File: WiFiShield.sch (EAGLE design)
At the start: 39 parts, among them IC1 74HC4050D, IC2 74AHC1G125, IC3 MCP9701A, IC4 SPX3819M5-L-3-3, IC5 CC3000MOD, J10 Test, J2 Mode, J3 Temp, J8 ARDUINO-SHIELD_R3, J9 U.FL-R-SMT-1(10)

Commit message: Fixups for MC74VHCT
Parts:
- IC1: value 74HC4050D -> MC74VHCT50A
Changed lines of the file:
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@@
 <part name="ANT1" library="adafruit" deviceset="ANTENNA" device=""/>
 <part name="U$2" library="freetronics-luke" deviceset="GND" device=""/>
-<part name="IC1" library="freetronics-angus" deviceset="MC74VHCT50A" device="" value="74HC4050D">
+<part name="IC1" library="freetronics-angus" deviceset="MC74VHCT50A" device="" value="MC74VHCT50A">
 <attribute name="PACKAGE" value="16-SOIC"/>
 </part>

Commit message: Remove temp sensor
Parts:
- removed IC3: MCP9701A, freetronics-master-v1:MCP9700SOT-23
- removed J3: Temp, freetronics-luke:SJ
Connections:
- removed net +5V-2: IC3.VDD, J8.+5V@0
- removed net N$11: IC3.OUT, J3.1
- new net N$3: IC1E.O
- net A0: no longer J3.2
- net CC3000_EN_3V3: no longer IC1E.O
- net GND: no longer IC3.GND
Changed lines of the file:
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@@
 <part name="J4" library="freetronics-master-v1.1" deviceset="M04" device="PTH"/>
 <part name="U$8" library="freetronics-luke" deviceset="+3.3V" device="" value="+3V3"/>
-<part name="IC3" library="freetronics-master-v1" deviceset="MCP9700" device="SOT-23" value="MCP9701A">
-<attribute name="PACKAGE" value="3-SOT23"/>
-</part>
-<part name="J3" library="freetronics-luke" deviceset="SJ" device="" value="Temp"/>
 <part name="S1" library="freetronics" deviceset="TAC_SWITCH" device="SMD" value="Reset"/>
-<part name="U$6" library="freetronics-luke" deviceset="GND" device=""/>
-<part name="U$9" library="freetronics-luke" deviceset="+5V" device=""/>
-<part name="U$11" library="freetronics-luke" deviceset="+5V" device=""/>
 <part name="U$12" library="freetronics-luke" deviceset="+3.3V" device="" value="+3V3"/>
 <part name="R5" library="freetronics-master-v1" deviceset="RESISTOR" device="0603" value="10k">
@@
 <attribute name="VALUE" x="40.64" y="175.26" size="1.27" layer="96" rot="MR0"/>
 </instance>
-<instance part="IC3" gate="G$1" x="88.9" y="20.32" smashed="yes">
-<attribute name="PACKAGE" x="76.2" y="30.48" size="1.27" layer="96"/>
-<attribute name="VALUE" x="76.2" y="33.02" size="1.27" layer="96"/>
-<attribute name="NAME" x="76.2" y="35.56" size="1.27" layer="95"/>
-</instance>
-<instance part="J3" gate="G$1" x="101.6" y="20.32" smashed="yes">
-<attribute name="NAME" x="101.6" y="15.24" size="1.27" layer="95"/>
-<attribute name="VALUE" x="101.6" y="12.7" size="1.27" layer="96"/>
-</instance>
 <instance part="S1" gate="S" x="218.44" y="101.6" smashed="yes">
 <attribute name="NAME" x="228.6" y="101.6" size="1.27" layer="95"/>
 <attribute name="VALUE" x="228.6" y="99.06" size="1.27" layer="96"/>
 </instance>
-<instance part="U$6" gate="G$1" x="99.06" y="10.16"/>
-<instance part="U$9" gate="G$1" x="99.06" y="30.48" rot="MR0"/>
-<instance part="U$11" gate="G$1" x="228.6" y="165.1"/>
 <instance part="U$12" gate="G$1" x="129.54" y="35.56" smashed="yes" rot="MR0">
 <attribute name="VALUE" x="127" y="35.56" size="1.27" layer="96" rot="MR0"/>
@@
 </segment>
 <segment>
-<pinref part="IC3" gate="G$1" pin="GND"/>
-<wire x1="96.52" y1="15.24" x2="99.06" y2="15.24" width="0.1524" layer="91"/>
-<pinref part="U$6" gate="G$1" pin="GND"/>
-<wire x1="99.06" y1="15.24" x2="99.06" y2="12.7" width="0.1524" layer="91"/>
-</segment>
-<segment>
 <pinref part="IC2" gate="P" pin="GND"/>
 <wire x1="25.4" y1="165.1" x2="22.86" y2="165.1" width="0.1524" layer="91"/>
@@
 <wire x1="223.52" y1="132.08" x2="205.74" y2="132.08" width="0.1524" layer="91"/>
 <label x="210.82" y="132.334" size="1.27" layer="95"/>
-</segment>
-<segment>
-<pinref part="J3" gate="G$1" pin="2"/>
-<wire x1="104.14" y1="20.32" x2="111.76" y2="20.32" width="0.1524" layer="91"/>
-<label x="106.68" y="20.574" size="1.27" layer="95"/>
 </segment>
 </net>
@@
 <net name="CC3000_EN_3V3" class="0">
 <segment>
-<pinref part="IC1" gate="E" pin="O"/>
-<wire x1="60.96" y1="15.24" x2="71.12" y2="15.24" width="0.1524" layer="91"/>
-<wire x1="71.12" y1="15.24" x2="71.12" y2="40.64" width="0.1524" layer="91"/>
-<wire x1="71.12" y1="40.64" x2="137.16" y2="40.64" width="0.1524" layer="91"/>
 <wire x1="137.16" y1="40.64" x2="172.72" y2="40.64" width="0.1524" layer="91"/>
 <wire x1="172.72" y1="40.64" x2="172.72" y2="63.5" width="0.1524" layer="91"/>
@@
 <wire x1="129.54" y1="17.78" x2="137.16" y2="17.78" width="0.1524" layer="91"/>
 <wire x1="137.16" y1="17.78" x2="137.16" y2="40.64" width="0.1524" layer="91"/>
-<junction x="137.16" y="40.64"/>
 </segment>
 </net>
@@
 </segment>
 </net>
-<net name="N$11" class="0">
-<segment>
-<pinref part="IC3" gate="G$1" pin="OUT"/>
-<wire x1="96.52" y1="20.32" x2="99.06" y2="20.32" width="0.1524" layer="91"/>
-<pinref part="J3" gate="G$1" pin="1"/>
-</segment>
-</net>
-<net name="+5V-2" class="0">
-<segment>
-<pinref part="J8" gate="G$1" pin="+5V@0"/>
-<pinref part="U$11" gate="G$1" pin="+5V"/>
-<wire x1="205.74" y1="160.02" x2="228.6" y2="160.02" width="0.1524" layer="91"/>
-<wire x1="228.6" y1="160.02" x2="228.6" y2="162.56" width="0.1524" layer="91"/>
-</segment>
-<segment>
-<pinref part="IC3" gate="G$1" pin="VDD"/>
-<wire x1="96.52" y1="25.4" x2="99.06" y2="25.4" width="0.1524" layer="91"/>
-<pinref part="U$9" gate="G$1" pin="+5V"/>
-<wire x1="99.06" y1="25.4" x2="99.06" y2="27.94" width="0.1524" layer="91"/>
-</segment>
-</net>
 <net name="!CC3000_CS_5V" class="0">
 <segment>
@@
 </segment>
 </net>
+<net name="N$3" class="0">
+<segment>
+<wire x1="71.12" y1="15.24" x2="71.12" y2="40.64" width="0.1524" layer="91"/>
+<pinref part="IC1" gate="E" pin="O"/>
+<wire x1="60.96" y1="15.24" x2="71.12" y2="15.24" width="0.1524" layer="91"/>
+</segment>
+</net>

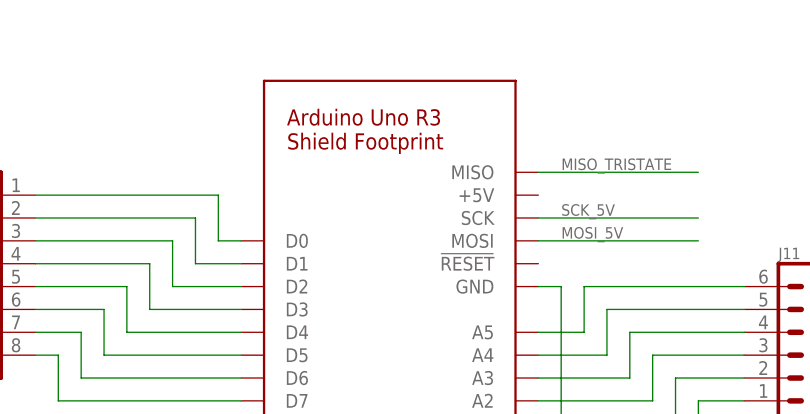
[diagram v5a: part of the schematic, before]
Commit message: Add silkscreen border
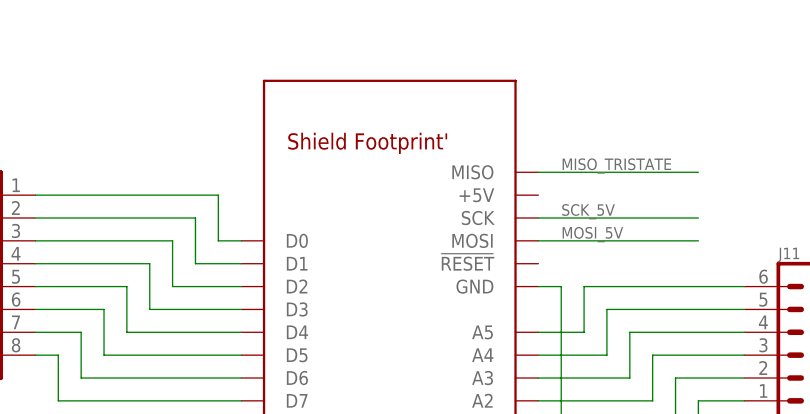
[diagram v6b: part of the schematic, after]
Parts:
- J8: device freetronics-luke:ARDUINO-SHIELD_R3 -> freetronics-angus:ARDUINO-SHIELD_R3
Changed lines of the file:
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@@
 </part>
 <part name="U$5" library="freetronics-luke" deviceset="GND" device=""/>
-<part name="J8" library="freetronics-luke" deviceset="ARDUINO-SHIELD_R3" device=""/>
+<part name="J8" library="freetronics-angus" deviceset="ARDUINO-SHIELD_R3" device=""/>
 <part name="U$21" library="freetronics-luke" deviceset="GND" device=""/>
 <part name="U$23" library="freetronics-luke" deviceset="GND" device=""/>

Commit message: Switch to chip antenna, final pre-prototype design review
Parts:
- removed R6, R7: 0R, freetronics-master-v1:RESISTOR0603
- ANT1: value ANTENNA -> 2500AT44M0400; device adafruit:ANTENNA -> freetronics-angus:2500AT44M0400
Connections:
- removed net N$15: IC5.SCL_CC3000, R6.2
- removed net N$5: IC5.SCL_EEPROM, R6.1
- net GND: no longer ANT1.GND
- net N$1: now also IC5.SDA_CC3000; no longer R7.2
- net N$104: now also ANT1.P$1; no longer ANT1.FEED
- net N$2: now also IC5.SCL_CC3000, IC5.SCL_EEPROM; no longer IC5.SDA_CC3000, R7.1
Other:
- note added: "50Ω 2.4 GHz Feed"
- note removed: "Meandered inverted-F antenna; 50Ω 2.4 GHz"
- moved on the sheet: J9
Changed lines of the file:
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@@
 <part name="IC5" library="freetronics-luke" deviceset="CC3000" device="" value="CC3000MOD"/>
 <part name="U$13" library="freetronics-luke" deviceset="GND" device=""/>
-<part name="R7" library="freetronics-master-v1" deviceset="RESISTOR" device="0603" value="0R">
-<attribute name="PACKAGE" value="0603"/>
-</part>
 <part name="C6" library="freetronics-master-v1" deviceset="CAP" device="0603" value="1uF">
 <attribute name="PACKAGE" value="0603"/>
 </part>
 <part name="+3V1" library="supply1" deviceset="+3V3" device="" value="+3V3"/>
-<part name="R6" library="freetronics-master-v1" deviceset="RESISTOR" device="0603" value="0R">
-<attribute name="PACKAGE" value="0603"/>
-</part>
 <part name="U$14" library="freetronics-luke" deviceset="GND" device=""/>
 <part name="L2" library="freetronics-master-v1" deviceset="INDUCTOR" device="0402" value="NP">
@@
 <attribute name="NOTE" value="NP"/>
 </part>
-<part name="ANT1" library="adafruit" deviceset="ANTENNA" device=""/>
 <part name="U$2" library="freetronics-luke" deviceset="GND" device=""/>
 <part name="IC1" library="freetronics-angus" deviceset="MC74VHCT50A" device="" value="MC74VHCT50A">
@@
 <part name="U$10" library="freetronics-luke" deviceset="GND" device=""/>
 <part name="U$27" library="freetronics-master-v1.1" deviceset="USD-SOCKET" device="NEW"/>
+<part name="ANT1" library="freetronics-angus" deviceset="2500AT44M0400" device=""/>
 </parts>
 <sheets>
@@
 <text x="68.58" y="88.9" size="1.27" layer="98">1-2: Test Mode
 2-3: Normal Mode</text>
-<text x="205.74" y="50.8" size="1.27" layer="98">Meandered inverted-F
-antenna; 50Ω 2.4 GHz</text>
+<text x="198.12" y="83.82" size="1.27" layer="98">50Ω 2.4 GHz Feed</text>
 <text x="205.74" y="167.64" size="1.27" layer="98">SPI lines connected to 6-pin ISP
 header for R3 compatibility.</text>
@@
 <instance part="IC5" gate="G$1" x="119.38" y="63.5"/>
 <instance part="U$13" gate="G$1" x="144.78" y="35.56"/>
-<instance part="R7" gate="G$1" x="160.02" y="68.58" smashed="yes" rot="R180">
-<attribute name="PACKAGE" x="172.72" y="68.58" size="1.27" layer="96"/>
-<attribute name="NAME" x="172.72" y="73.66" size="1.27" layer="95"/>
-<attribute name="VALUE" x="172.72" y="71.12" size="1.27" layer="96"/>
-</instance>
 <instance part="C6" gate="G$1" x="152.4" y="48.26" smashed="yes" rot="R180">
 <attribute name="NAME" x="157.48" y="50.8" size="1.27" layer="95"/>
@@
 <instance part="+3V1" gate="G$1" x="152.4" y="83.82" smashed="yes">
 <attribute name="VALUE" x="144.78" y="83.82" size="1.27" layer="96"/>
-</instance>
-<instance part="R6" gate="G$1" x="160.02" y="76.2" smashed="yes" rot="R180">
-<attribute name="PACKAGE" x="157.48" y="81.28" size="1.27" layer="96"/>
-<attribute name="NAME" x="157.48" y="86.36" size="1.27" layer="95"/>
-<attribute name="VALUE" x="157.48" y="83.82" size="1.27" layer="96"/>
 </instance>
 <instance part="U$14" gate="G$1" x="152.4" y="35.56"/>
@@
 <attribute name="PACKAGE" x="187.96" y="81.28" size="1.27" layer="96"/>
 </instance>
-<instance part="J9" gate="G$1" x="208.28" y="78.74" smashed="yes" rot="MR0">
-<attribute name="VALUE" x="213.36" y="78.74" size="1.27" layer="96"/>
-<attribute name="NAME" x="213.36" y="81.28" size="1.27" layer="95"/>
-<attribute name="NOTE" x="213.36" y="76.2" size="1.27" layer="96"/>
-</instance>
-<instance part="ANT1" gate="G$1" x="208.28" y="60.96" rot="R270"/>
+<instance part="J9" gate="G$1" x="215.9" y="78.74" smashed="yes" rot="MR0">
+<attribute name="VALUE" x="220.98" y="78.74" size="1.27" layer="96"/>
+<attribute name="NAME" x="220.98" y="81.28" size="1.27" layer="95"/>
+<attribute name="NOTE" x="220.98" y="76.2" size="1.27" layer="96"/>
+</instance>
 <instance part="U$2" gate="G$1" x="40.64" y="104.14" rot="MR0"/>
 <instance part="IC1" gate="F" x="50.8" y="27.94" smashed="yes" rot="R180">
@@
 <instance part="U$10" gate="G$1" x="22.86" y="160.02" rot="MR0"/>
 <instance part="U$27" gate="G$1" x="22.86" y="129.54" rot="MR0"/>
+<instance part="ANT1" gate="G$1" x="218.44" y="60.96" smashed="yes" rot="MR0">
+<attribute name="NAME" x="220.98" y="60.96" size="1.27" layer="95" rot="MR0" align="bottom-right"/>
+<attribute name="VALUE" x="220.98" y="58.42" size="1.27" layer="96" rot="MR0" align="bottom-right"/>
+</instance>
 </instances>
 <busses>
@@
 <segment>
 <pinref part="U$22" gate="G$1" pin="GND"/>
-<wire x1="203.2" y1="58.42" x2="203.2" y2="40.64" width="0.1524" layer="91"/>
 <pinref part="J9" gate="G$1" pin="GND"/>
-<wire x1="205.74" y1="76.2" x2="203.2" y2="76.2" width="0.1524" layer="91"/>
-<wire x1="203.2" y1="76.2" x2="203.2" y2="58.42" width="0.1524" layer="91"/>
-<pinref part="ANT1" gate="G$1" pin="GND"/>
-<wire x1="208.28" y1="58.42" x2="203.2" y2="58.42" width="0.1524" layer="91"/>
-<junction x="203.2" y="58.42"/>
+<wire x1="213.36" y1="76.2" x2="203.2" y2="76.2" width="0.1524" layer="91"/>
+<wire x1="203.2" y1="76.2" x2="203.2" y2="40.64" width="0.1524" layer="91"/>
 </segment>
 <segment>
@@
 </segment>
 </net>
-<net name="N$1" class="0">
-<segment>
-<pinref part="IC5" gate="G$1" pin="SDA_EEPROM"/>
-<pinref part="R7" gate="G$1" pin="2"/>
-<wire x1="142.24" y1="68.58" x2="154.94" y2="68.58" width="0.1524" layer="91"/>
-</segment>
-</net>
-<net name="N$2" class="0">
-<segment>
-<pinref part="IC5" gate="G$1" pin="SDA_CC3000"/>
-<wire x1="142.24" y1="73.66" x2="167.64" y2="73.66" width="0.1524" layer="91"/>
-<wire x1="167.64" y1="73.66" x2="170.18" y2="71.12" width="0.1524" layer="91"/>
-<pinref part="R7" gate="G$1" pin="1"/>
-<wire x1="165.1" y1="68.58" x2="170.18" y2="68.58" width="0.1524" layer="91"/>
-<wire x1="170.18" y1="68.58" x2="170.18" y2="71.12" width="0.1524" layer="91"/>
-</segment>
-</net>
-<net name="N$5" class="0">
-<segment>
-<pinref part="IC5" gate="G$1" pin="SCL_EEPROM"/>
-<wire x1="142.24" y1="71.12" x2="167.64" y2="71.12" width="0.1524" layer="91"/>
-<wire x1="167.64" y1="71.12" x2="170.18" y2="73.66" width="0.1524" layer="91"/>
-<pinref part="R6" gate="G$1" pin="1"/>
-<wire x1="165.1" y1="76.2" x2="170.18" y2="76.2" width="0.1524" layer="91"/>
-<wire x1="170.18" y1="76.2" x2="170.18" y2="73.66" width="0.1524" layer="91"/>
-</segment>
-</net>
-<net name="N$15" class="0">
-<segment>
-<pinref part="IC5" gate="G$1" pin="SCL_CC3000"/>
-<pinref part="R6" gate="G$1" pin="2"/>
-<wire x1="142.24" y1="76.2" x2="154.94" y2="76.2" width="0.1524" layer="91"/>
-</segment>
-</net>
 <net name="WL_EN2" class="0">
 <segment>
@@
 <wire x1="195.58" y1="60.96" x2="208.28" y2="60.96" width="0.1524" layer="91"/>
 <junction x="195.58" y="60.96"/>
-<pinref part="ANT1" gate="G$1" pin="FEED"/>
+<pinref part="ANT1" gate="G$1" pin="P$1"/>
 </segment>
 </net>
@@
 <pinref part="C9" gate="G$1" pin="1"/>
 <pinref part="J9" gate="G$1" pin="SIG"/>
-<wire x1="205.74" y1="78.74" x2="198.12" y2="78.74" width="0.1524" layer="91"/>
+<wire x1="213.36" y1="78.74" x2="198.12" y2="78.74" width="0.1524" layer="91"/>
 </segment>
 </net>
@@
 </segment>
 </net>
+<net name="N$1" class="0">
+<segment>
+<pinref part="IC5" gate="G$1" pin="SDA_EEPROM"/>
+<wire x1="142.24" y1="68.58" x2="149.86" y2="68.58" width="0.1524" layer="91"/>
+<wire x1="149.86" y1="68.58" x2="149.86" y2="73.66" width="0.1524" layer="91"/>
+<pinref part="IC5" gate="G$1" pin="SDA_CC3000"/>
+<wire x1="149.86" y1="73.66" x2="142.24" y2="73.66" width="0.1524" layer="91"/>
+</segment>
+</net>
+<net name="N$2" class="0">
+<segment>
+<pinref part="IC5" gate="G$1" pin="SCL_EEPROM"/>
+<wire x1="142.24" y1="71.12" x2="147.32" y2="71.12" width="0.1524" layer="91"/>
+<wire x1="147.32" y1="71.12" x2="147.32" y2="76.2" width="0.1524" layer="91"/>
+<pinref part="IC5" gate="G$1" pin="SCL_CC3000"/>
+<wire x1="147.32" y1="76.2" x2="142.24" y2="76.2" width="0.1524" layer="91"/>
+</segment>
+</net>

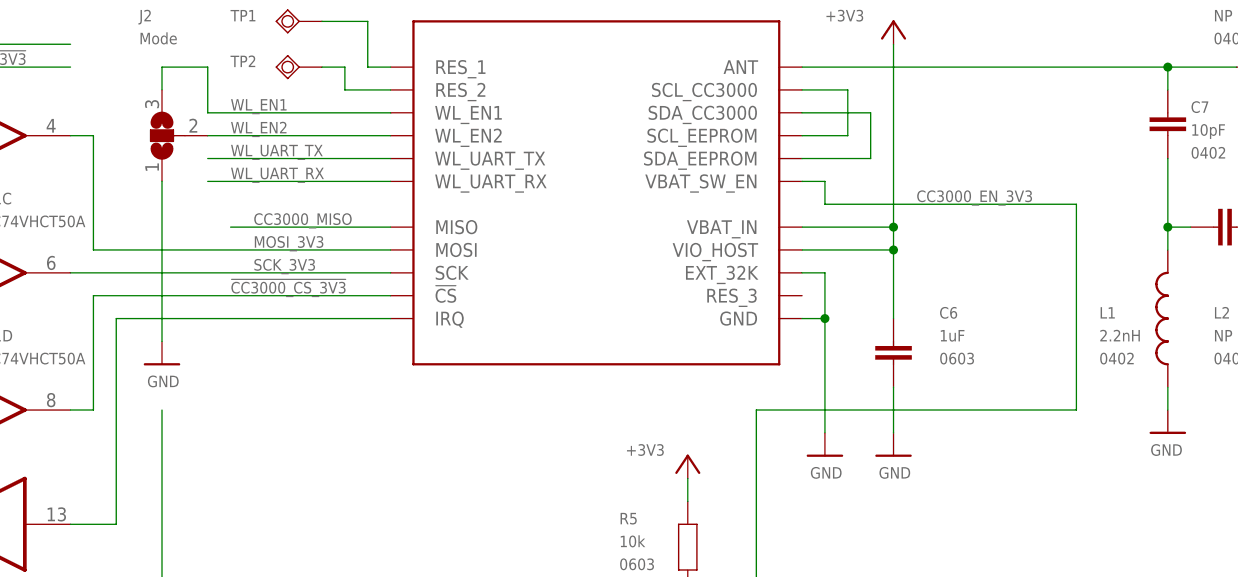
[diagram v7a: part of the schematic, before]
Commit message: Replace accidentally deleted wire
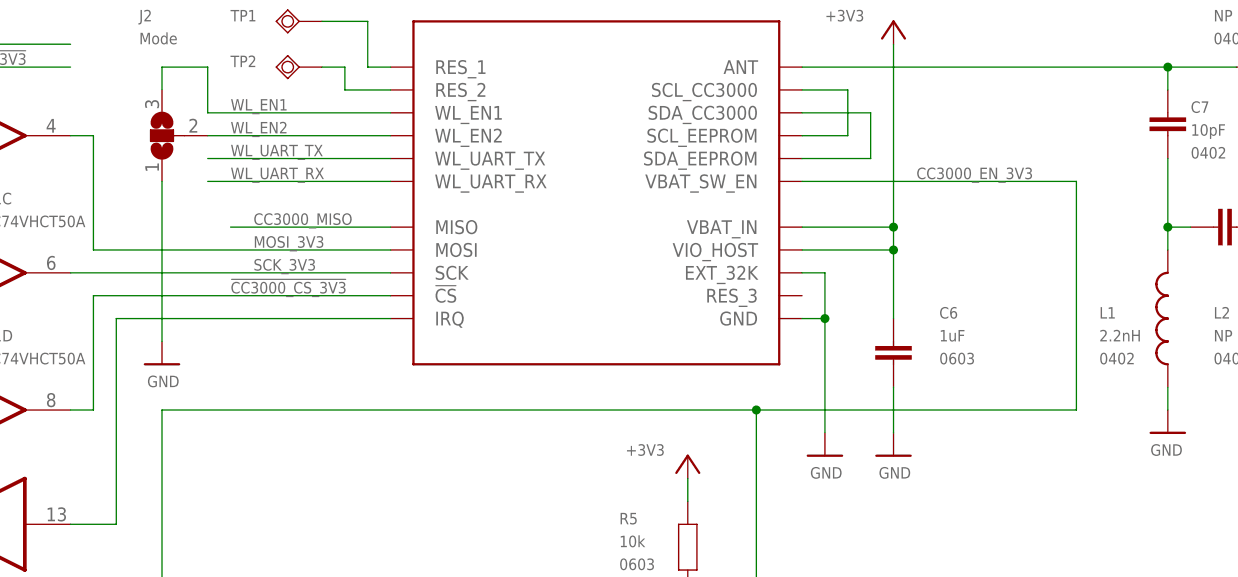
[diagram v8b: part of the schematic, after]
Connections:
- removed net N$3: IC1E.O
- net CC3000_EN_3V3: now also IC1E.O
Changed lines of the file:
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@@
 <segment>
 <wire x1="137.16" y1="40.64" x2="172.72" y2="40.64" width="0.1524" layer="91"/>
-<wire x1="172.72" y1="40.64" x2="172.72" y2="63.5" width="0.1524" layer="91"/>
-<wire x1="172.72" y1="63.5" x2="144.78" y2="63.5" width="0.1524" layer="91"/>
-<wire x1="144.78" y1="63.5" x2="144.78" y2="66.04" width="0.1524" layer="91"/>
+<wire x1="172.72" y1="40.64" x2="172.72" y2="66.04" width="0.1524" layer="91"/>
 <pinref part="IC5" gate="G$1" pin="VBAT_SW_EN"/>
-<wire x1="144.78" y1="66.04" x2="142.24" y2="66.04" width="0.1524" layer="91"/>
-<label x="154.94" y="63.754" size="1.27" layer="95"/>
+<label x="154.94" y="66.294" size="1.27" layer="95"/>
 <pinref part="R5" gate="G$1" pin="2"/>
 <wire x1="129.54" y1="20.32" x2="129.54" y2="17.78" width="0.1524" layer="91"/>
 <wire x1="129.54" y1="17.78" x2="137.16" y2="17.78" width="0.1524" layer="91"/>
 <wire x1="137.16" y1="17.78" x2="137.16" y2="40.64" width="0.1524" layer="91"/>
+<wire x1="71.12" y1="15.24" x2="71.12" y2="40.64" width="0.1524" layer="91"/>
+<pinref part="IC1" gate="E" pin="O"/>
+<wire x1="60.96" y1="15.24" x2="71.12" y2="15.24" width="0.1524" layer="91"/>
+<wire x1="71.12" y1="40.64" x2="137.16" y2="40.64" width="0.1524" layer="91"/>
+<junction x="137.16" y="40.64"/>
+<wire x1="142.24" y1="66.04" x2="172.72" y2="66.04" width="0.1524" layer="91"/>
 </segment>
 </net>
@@
 </segment>
 </net>
-<net name="N$3" class="0">
-<segment>
-<wire x1="71.12" y1="15.24" x2="71.12" y2="40.64" width="0.1524" layer="91"/>
-<pinref part="IC1" gate="E" pin="O"/>
-<wire x1="60.96" y1="15.24" x2="71.12" y2="15.24" width="0.1524" layer="91"/>
-</segment>
-</net>
